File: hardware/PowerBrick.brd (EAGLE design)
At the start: 27.6 x 14 mm, 18 parts, among them Q1 SI2308BDS-T1-GE3, Q2 SI2308BDS-T1-GE3, U1 PIC12F615SN, U2 LK112M50TR, U3 BD6221

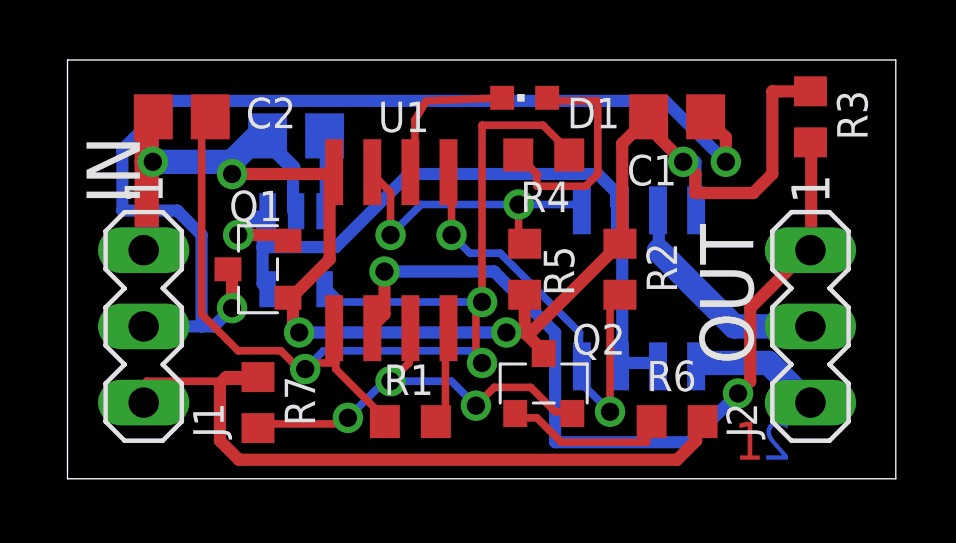
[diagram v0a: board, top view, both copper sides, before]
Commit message: Added optional level shift transistor on the receiver PWM input
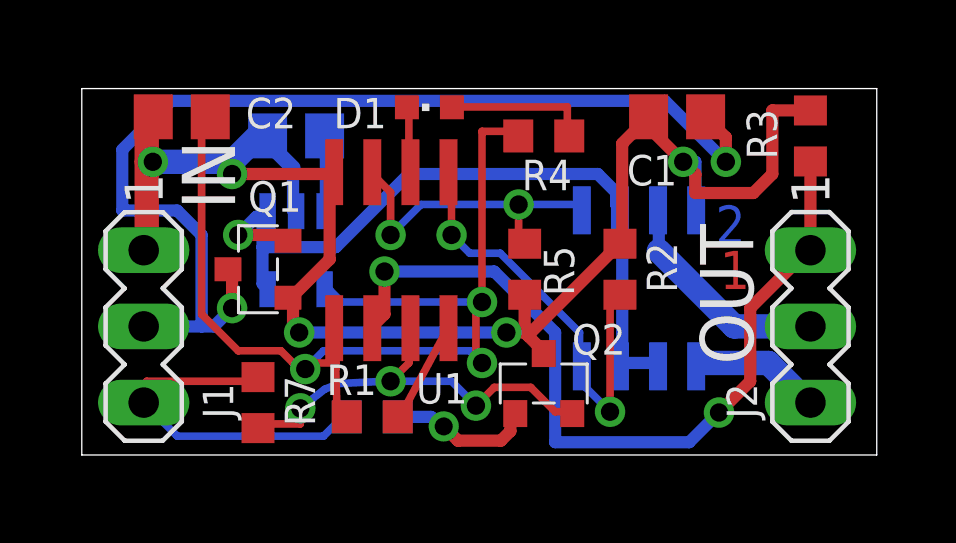
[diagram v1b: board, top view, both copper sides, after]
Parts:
- moved R6 10.2 mm to (10.2, 2.06), flipped to the bottom
- moved D1 3.19 mm to (12.1, 12.4)
- moved R1 1.28 mm to (10.2, 2.06)
- moved R3 0.63 mm to (24.8, 11.4)
- moved R4 0.63 mm to (15.9, 11.4), turned to 0 degrees
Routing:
- net N$13: track 24.9 -> 12.0 mm
- net N$9: track 5.52 -> 2.39 mm
- net N$3: track 39.0 -> 36.0 mm
- net N$8: track 7.68 -> 4.83 mm
- net N$1: track 28.4 -> 27.7 mm
- net GND: track 52.9 -> 52.3 mm
- net N$12: track 5.58 -> 5.12 mm, vias 0 -> 1
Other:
- board size 27.6 x 14 mm -> 26.5 x 12.2 mm
